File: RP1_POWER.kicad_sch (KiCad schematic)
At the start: 60 parts, among them U3 RP1

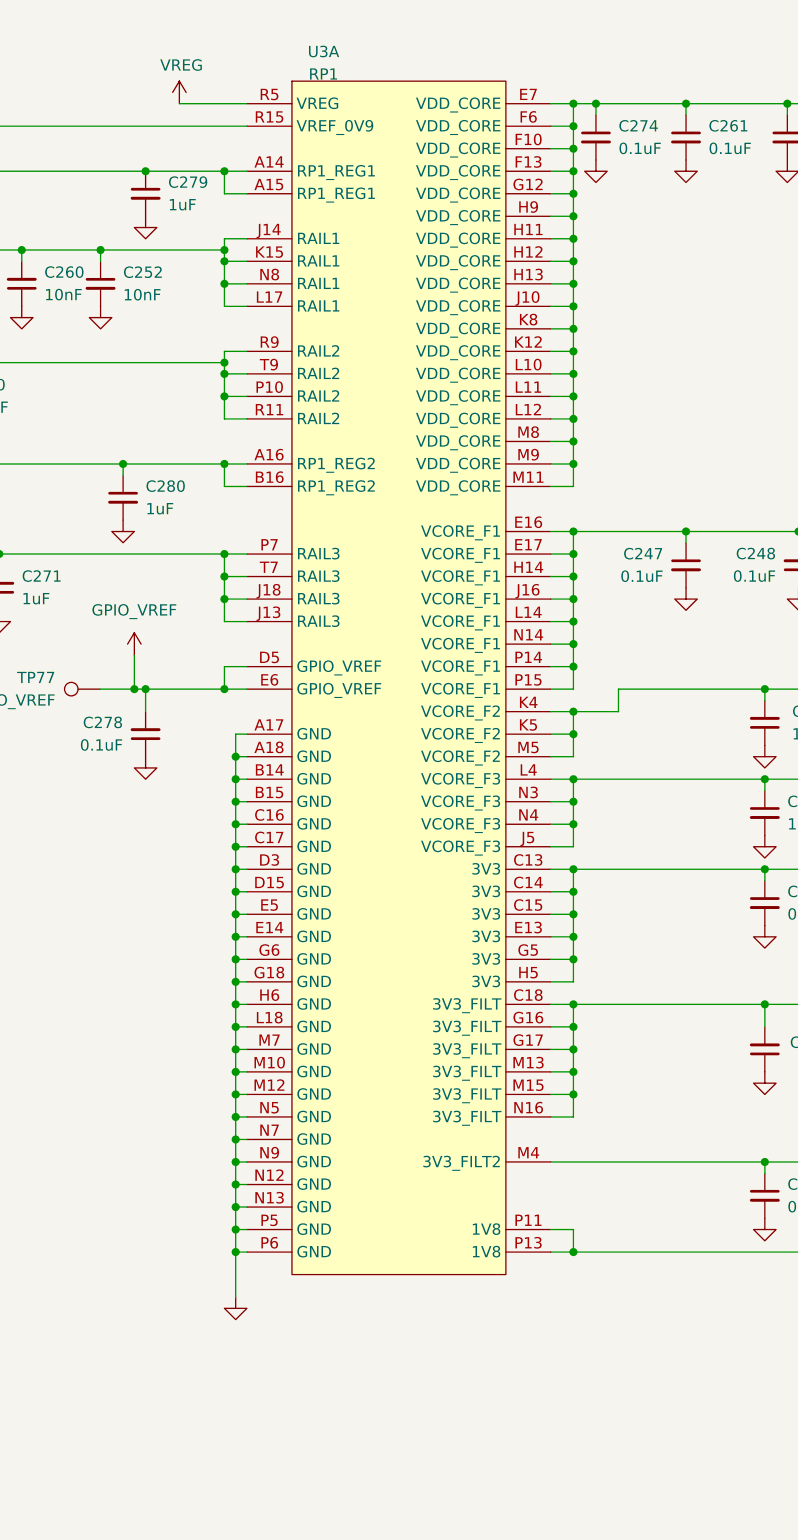
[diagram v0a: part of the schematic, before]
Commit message: Add RP1 grounds. Identify PCIe clock
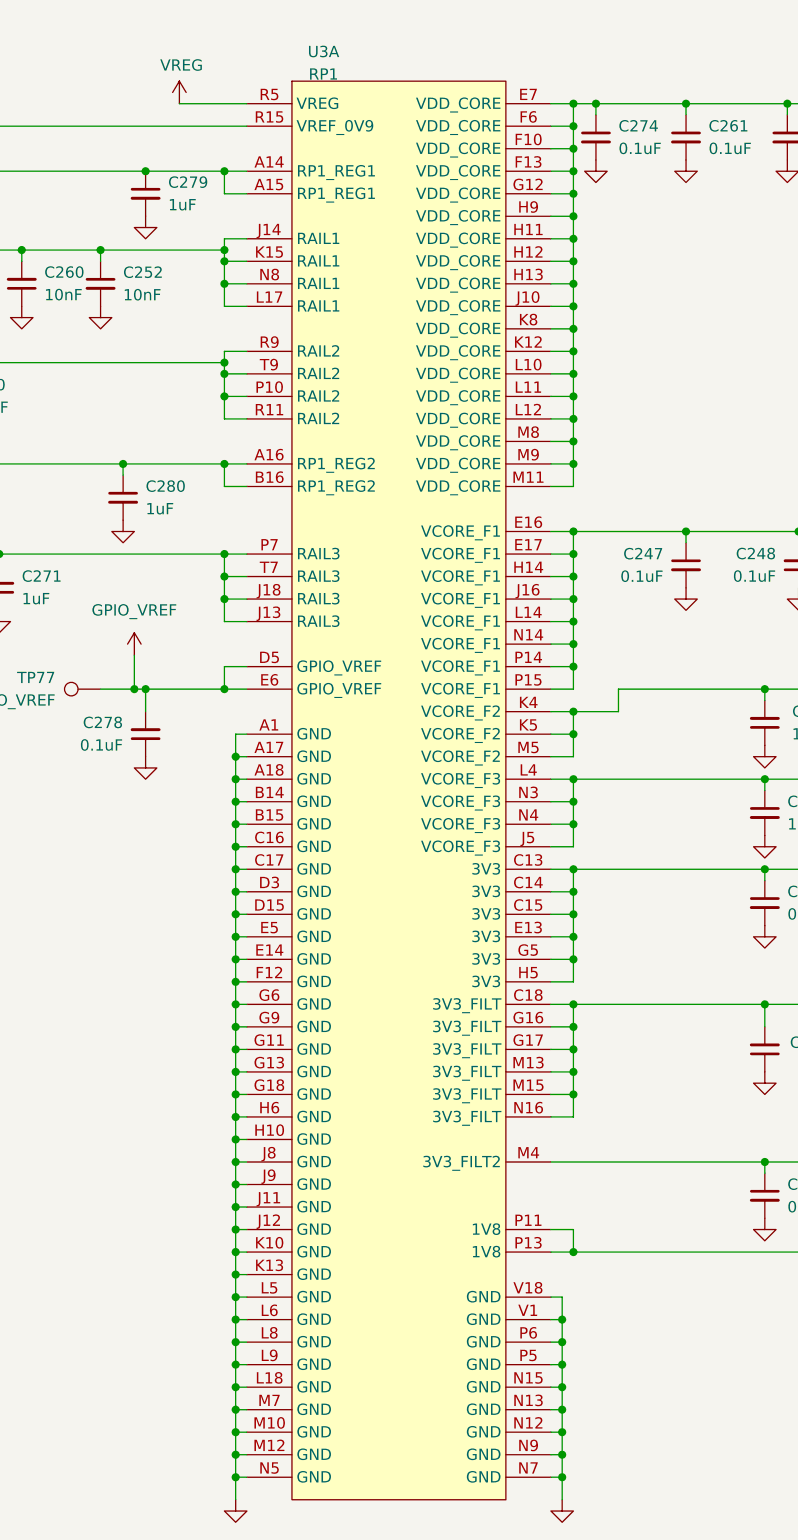
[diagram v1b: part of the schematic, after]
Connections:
- net GND: now also U3.A1 (GND), U3.F12 (GND), U3.G11 (GND), U3.G13 (GND), U3.G9 (GND), U3.H10 (GND), U3.J11 (GND), U3.J12 (GND), U3.J8 (GND), U3.J9 (GND), U3.K10 (GND), U3.K13 (GND), U3.L5 (GND), U3.L6 (GND), U3.L8 (GND), U3.L9 (GND), U3.N15 (GND), U3.V1 (GND), U3.V18 (GND)
